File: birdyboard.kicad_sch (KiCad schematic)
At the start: 52 parts, among them J1 JST_3pin, J10 Conn_02x20_Odd_Even, J11 JST-PH StepMotor Conn, J12 TBP02R2-381-04BE, J13 Screw_Terminal_01x02, J14 Screw_Terminal_01x02, J15 Screw_Terminal_01x02, J16 JST-PH StepMotor Conn, J17 TBP02R2-381-04BE, J18 JST-PH StepMotor Conn, J19 TBP02R2-381-04BE, J2 JST_3pin, J20 JST-PH StepMotor Conn, J21 JST-PH UART Conn, J22 TBP02R2-381-04BE, J23 Conn_01x10, J24 AS5047_Adapter_Board_Connector, J25 AS5047_Adapter_Board_Connector, J26 AS5047_Adapter_Board_Connector, J27 AS5047_Adapter_Board_Connector, J4 JST_3pin, J5 JST_3pin, J6 JST_3pin, J7 JST_3pin, J8 JST_3pin, J9 JST_3pin, U1 TMC2209_SILENTSTEPSTICK, U2 TMC2209_SILENTSTEPSTICK, U3 Pico, U4 TMC2209_SILENTSTEPSTICK, U5 TMC2209_SILENTSTEPSTICK, U6 SN74CBT3253 MUX/DEMUX, U7 AZ1117CH-3_3TRG1, U8 K7805-3AR3

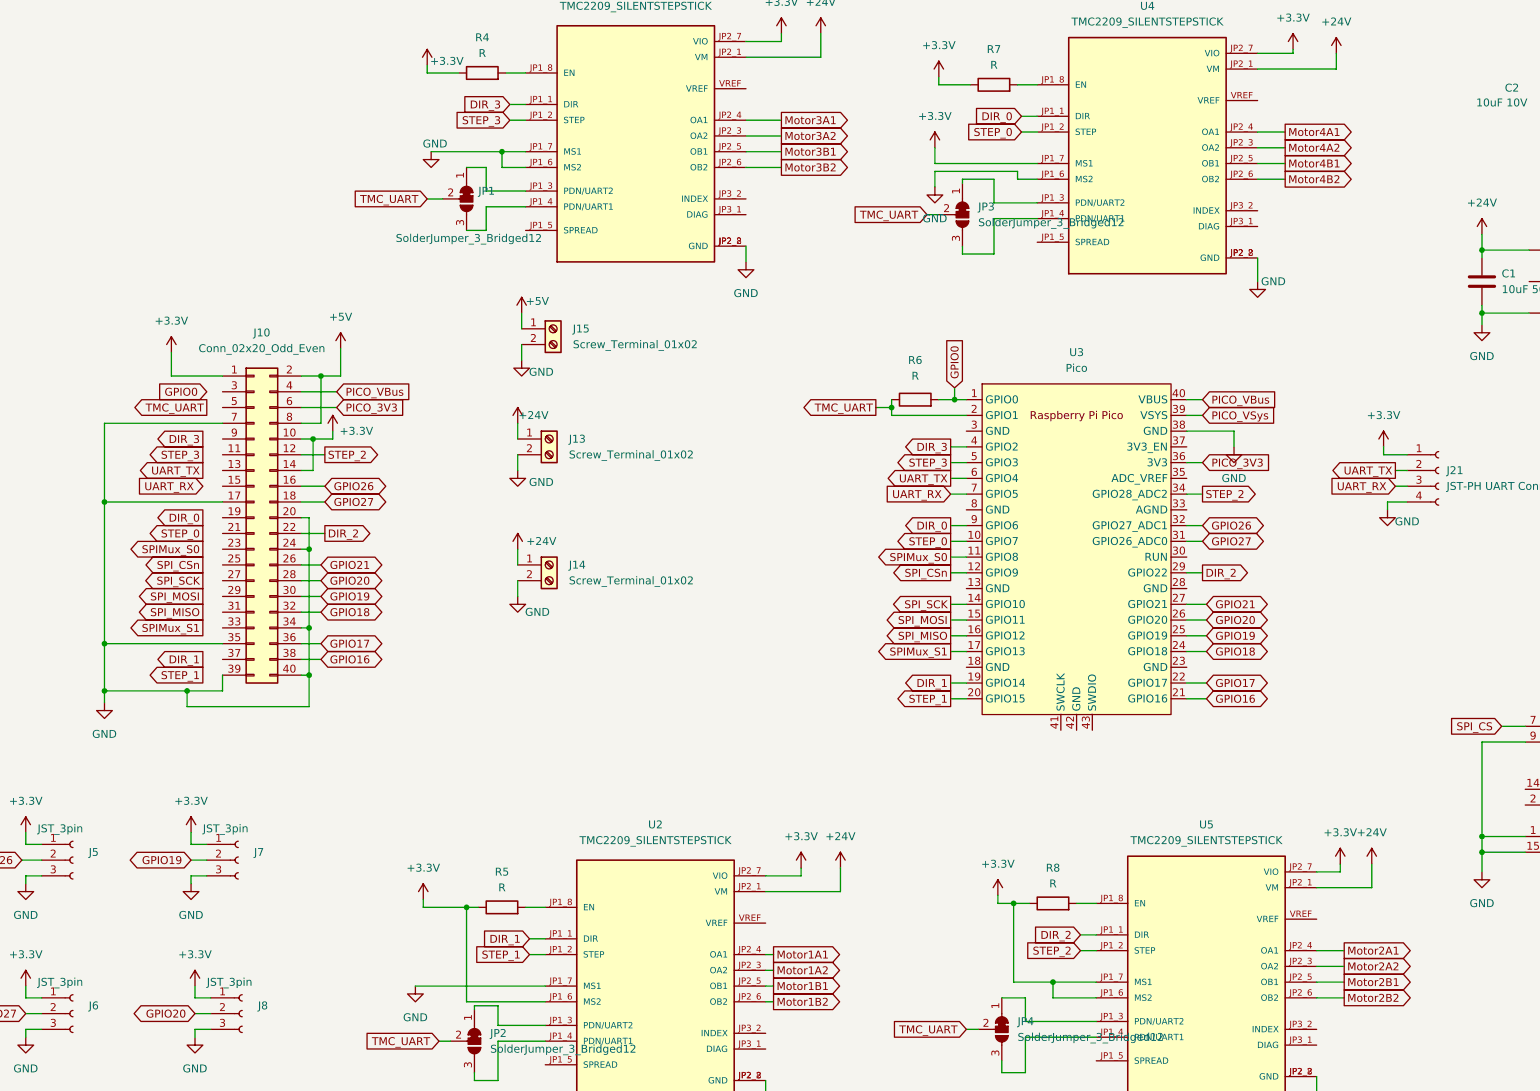
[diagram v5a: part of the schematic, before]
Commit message: -- Adds copper pours -- Adds netclasses & constraints for each netclasses -- Adds some pcb routes for some connections
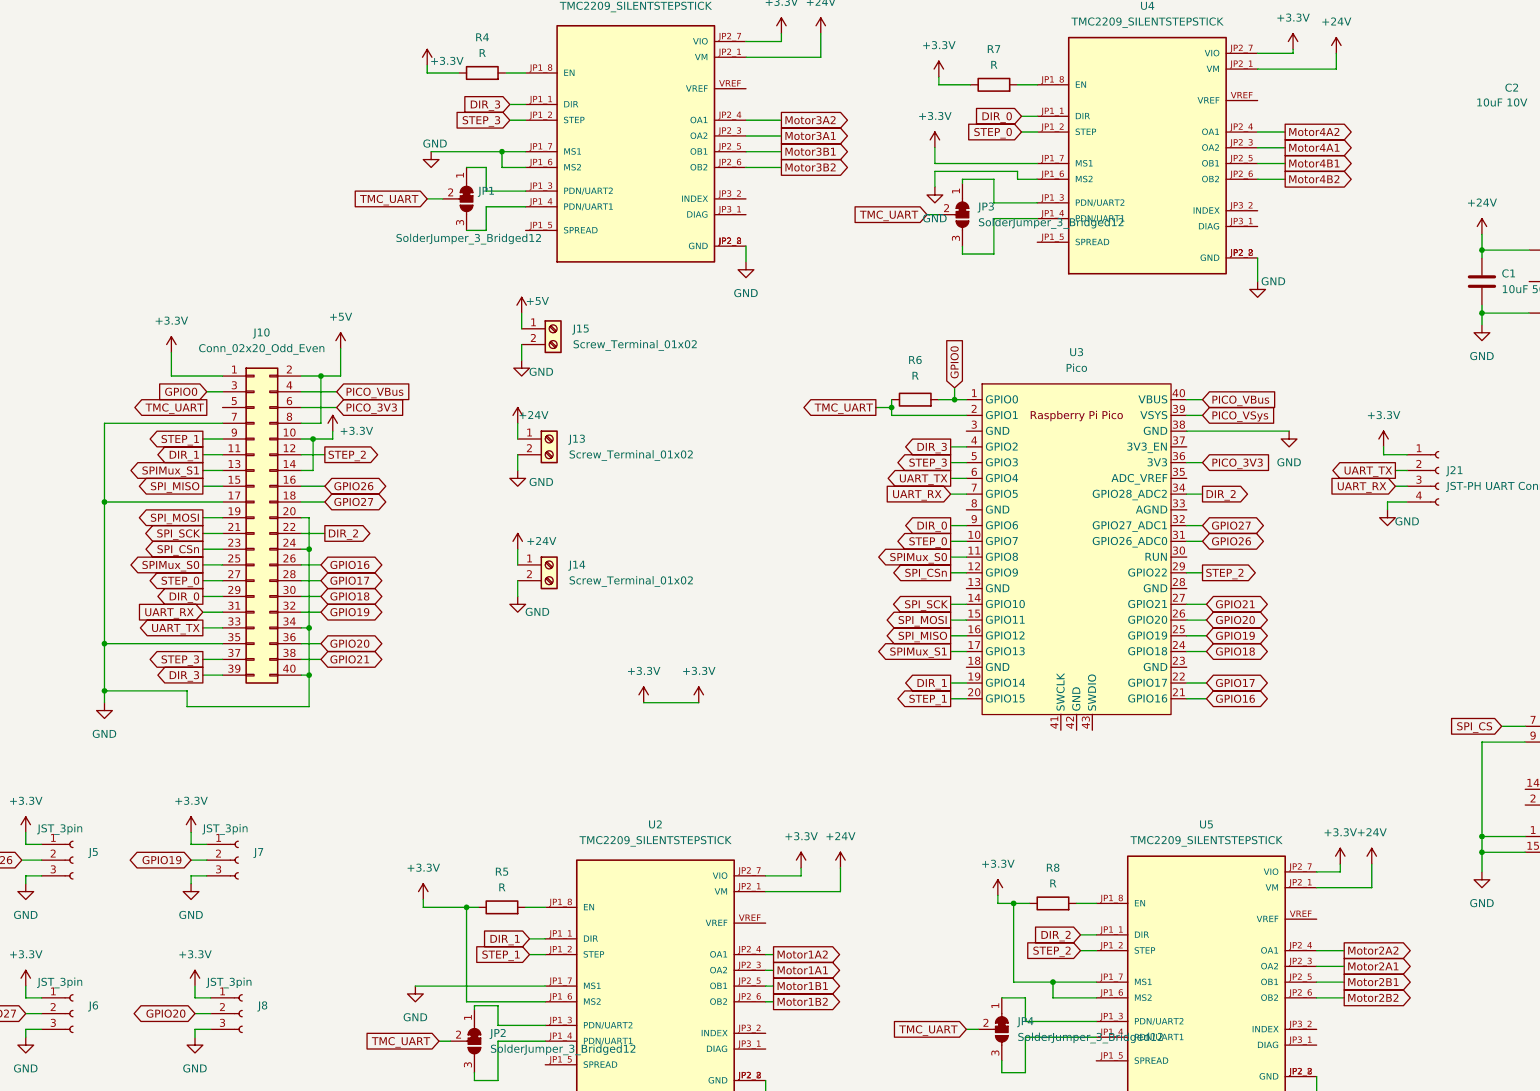
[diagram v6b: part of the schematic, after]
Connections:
- net +3V3 is gone; now on net +3.3V: J1.1 (Pin_1), J2.1 (Pin_1), J24.3 (Pin_3), J4.1 (Pin_1), J5.1 (Pin_1), J6.1 (Pin_1), J7.1 (Pin_1), J8.1 (Pin_1), J9.1 (Pin_1), R1.1, R2.1, R3.1, R4.1, R5.1, R7.1, R8.1, U1.JP2_7 (VIO), U2.JP1_6 (MS2), U2.JP2_7 (VIO), U4.JP1_7 (MS1), U4.JP2_7 (VIO), U5.JP1_6 (MS2), U5.JP1_7 (MS1), U5.JP2_7 (VIO), U6.16 (VCC)
- net DIR_0: now also J10.29 (Pin_29)
- net DIR_1: now also J10.11 (Pin_11)
- net DIR_2: now also U3.34 (GPIO28_ADC2); no longer U3.29 (GPIO22)
- net DIR_3: now also J10.39 (Pin_39)
- net GND: no longer J10.39 (Pin_39)
- net GPIO0: now also J10.3 (Pin_3)
- net GPIO16: now also J10.26 (Pin_26); no longer J10.38 (Pin_38)
- net GPIO17: now also J10.28 (Pin_28); no longer J10.36 (Pin_36)
- net GPIO18: now also J10.30 (Pin_30); no longer J10.32 (Pin_32)
- net GPIO19: now also J10.32 (Pin_32); no longer J10.30 (Pin_30)
- net GPIO20: now also J10.36 (Pin_36); no longer J10.28 (Pin_28)
- net GPIO21: now also J10.38 (Pin_38); no longer J10.26 (Pin_26)
- net GPIO26: now also U3.31 (GPIO26_ADC0); no longer U3.32 (GPIO27_ADC1)
- net GPIO27: now also U3.32 (GPIO27_ADC1); no longer U3.31 (GPIO26_ADC0)
- net Motor1A1: now also U2.JP2_3 (OA2); no longer U2.JP2_4 (OA1)
- net Motor1A2: now also U2.JP2_4 (OA1); no longer U2.JP2_3 (OA2)
- net Motor2A1: now also U5.JP2_3 (OA2); no longer U5.JP2_4 (OA1)
- net Motor2A2: now also U5.JP2_4 (OA1); no longer U5.JP2_3 (OA2)
- net Motor3A1: now also U1.JP2_3 (OA2); no longer U1.JP2_4 (OA1)
- net Motor3A2: now also U1.JP2_4 (OA1); no longer U1.JP2_3 (OA2)
- net Motor4A1: now also U4.JP2_3 (OA2); no longer U4.JP2_4 (OA1)
- net Motor4A2: now also U4.JP2_4 (OA1); no longer U4.JP2_3 (OA2)
- net SPIMux_S0: now also J10.25 (Pin_25)
- net SPIMux_S1: now also J10.13 (Pin_13)
- net SPI_CSn: now also J10.23 (Pin_23)
- net SPI_MISO: now also J10.15 (Pin_15)
- net SPI_MOSI: now also J10.19 (Pin_19)
- net SPI_SCK: now also J10.21 (Pin_21)
- net STEP_0: now also J10.27 (Pin_27)
- net STEP_1: now also J10.9 (Pin_9)
- net STEP_2: now also U3.29 (GPIO22); no longer U3.34 (GPIO28_ADC2)
- net STEP_3: now also J10.37 (Pin_37)
- net UART_RX: now also J10.31 (Pin_31)
- net UART_TX: now also J10.33 (Pin_33)

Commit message: lay out some routes - place last components
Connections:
- net ENC_CS_1: now also U6.6 (1B1)
- net ENC_CS_1_Muxed: no longer U6.6 (1B1)
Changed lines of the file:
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@@
     )
   )
-  (global_label "ENC_CS_1_Muxed" (shape output) (at 207.01 132.715 0) (fields_autoplaced)
+  (global_label "ENC_CS_1" (shape output) (at 207.01 132.715 0) (fields_autoplaced)
     (effects (font (size 1.27 1.27)) (justify left))
-    (property "Intersheet References" "${INTERSHEET_REFS}" (id 0) (at 225.6307 132.6356 0)
+    (property "Intersheet References" "${INTERSHEET_REFS}" (id 0) (at 218.7969 132.6356 0)
       (effects (font (size 1.27 1.27)) (justify left) hide)
     )

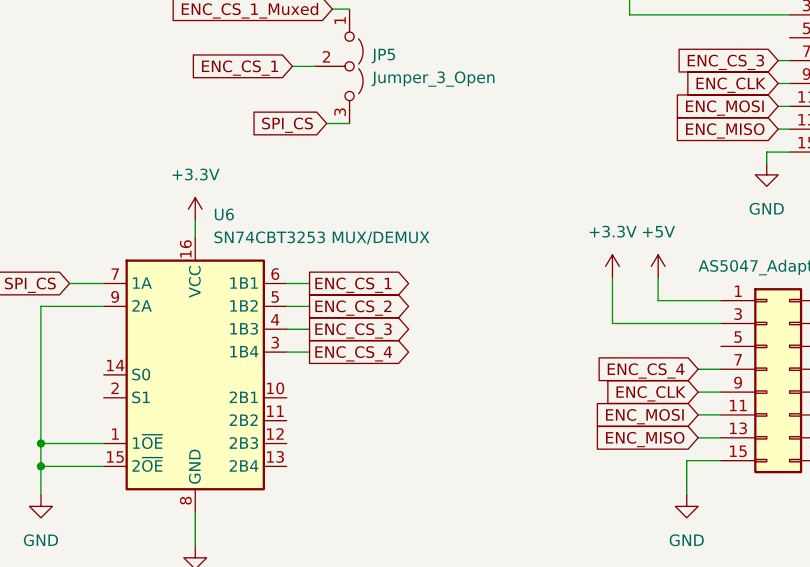
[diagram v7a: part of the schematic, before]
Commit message: connects up the PCB Layout
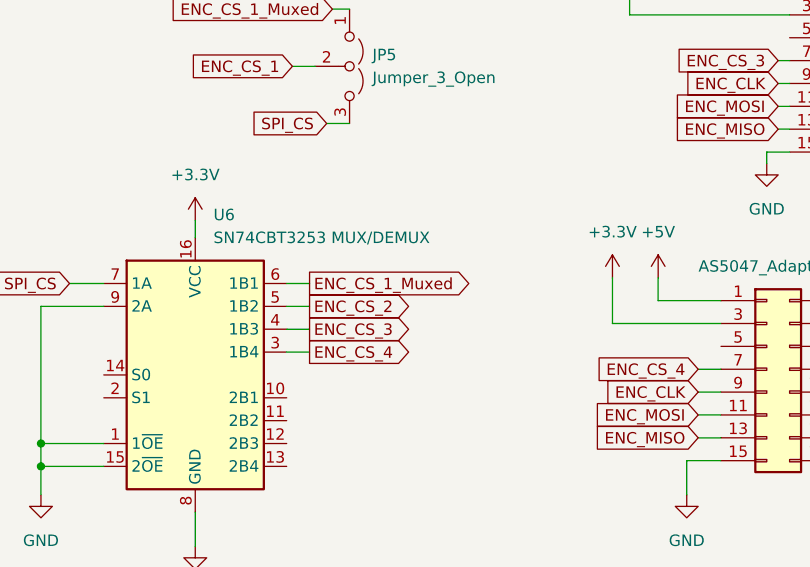
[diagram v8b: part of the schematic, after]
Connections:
- net ENC_CS_1: no longer U6.6 (1B1)
- net ENC_CS_1_Muxed: now also U6.6 (1B1)
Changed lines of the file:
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@@
     )
   )
-  (global_label "ENC_CS_1" (shape output) (at 207.01 132.715 0) (fields_autoplaced)
+  (global_label "ENC_CS_1_Muxed" (shape output) (at 207.01 132.715 0) (fields_autoplaced)
     (effects (font (size 1.27 1.27)) (justify left))
-    (property "Intersheet References" "${INTERSHEET_REFS}" (id 0) (at 218.7969 132.6356 0)
+    (property "Intersheet References" "${INTERSHEET_REFS}" (id 0) (at 225.6307 132.6356 0)
       (effects (font (size 1.27 1.27)) (justify left) hide)
     )
@@
   (symbol (lib_name "+3.3V_1") (lib_id "power:+3.3V") (at 50.8 128.905 0) (unit 1)
     (in_bom yes) (on_board yes) (fields_autoplaced)
-    (property "Reference" "#PWR?" (id 0) (at 50.8 132.715 0)
+    (property "Reference" "#PWR0102" (id 0) (at 50.8 132.715 0)
       (effects (font (size 1.27 1.27)) hide)
     )
@@
   (symbol (lib_id "power:+3.3V") (at 41.91 128.905 0) (unit 1)
     (in_bom yes) (on_board yes) (fields_autoplaced)
-    (property "Reference" "#PWR?" (id 0) (at 41.91 132.715 0)
+    (property "Reference" "#PWR0101" (id 0) (at 41.91 132.715 0)
       (effects (font (size 1.27 1.27)) hide)
     )
@@
       (reference "#PWR078") (unit 1) (value "GND") (footprint "")
     )
+    (path "/eda659b2-1925-4ab5-9f1a-b47d20317b89"
+      (reference "#PWR0101") (unit 1) (value "+3.3V") (footprint "")
+    )
     (path "/1968f49d-c12c-4cd8-84b6-5a09f3a03fc0"
-      (reference "#PWR?") (unit 1) (value "+3.3V") (footprint "")
-    )
-    (path "/eda659b2-1925-4ab5-9f1a-b47d20317b89"
-      (reference "#PWR?") (unit 1) (value "+3.3V") (footprint "")
+      (reference "#PWR0102") (unit 1) (value "+3.3V") (footprint "")
     )
     (path "/fa1d0df7-b404-4cc1-bb33-a02815905db3"
